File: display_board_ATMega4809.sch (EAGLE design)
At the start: 38 parts, among them J2 LD09P33E4GV00LF, J3 SULLINS_NREC005SABC-M30RCSULL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, SW1 TE_CONNECTIVITY_FSM2JSMAATE_C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, SW2 TE_CONNECTIVITY_FSM2JSMAATE_C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, SW3 TE_CONNECTIVITY_FSM2JSMAATE_C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, SW4 TE_CONNECTIVITY_FSM2JSMAATE_C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, U1 LSF0102DCTR, U2 MCP1703AT-5002E_CB, U3 MCP1801T-3302I_OT, U4 SI2323DDS-T1-GE3SOT_DS-T1-GE3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

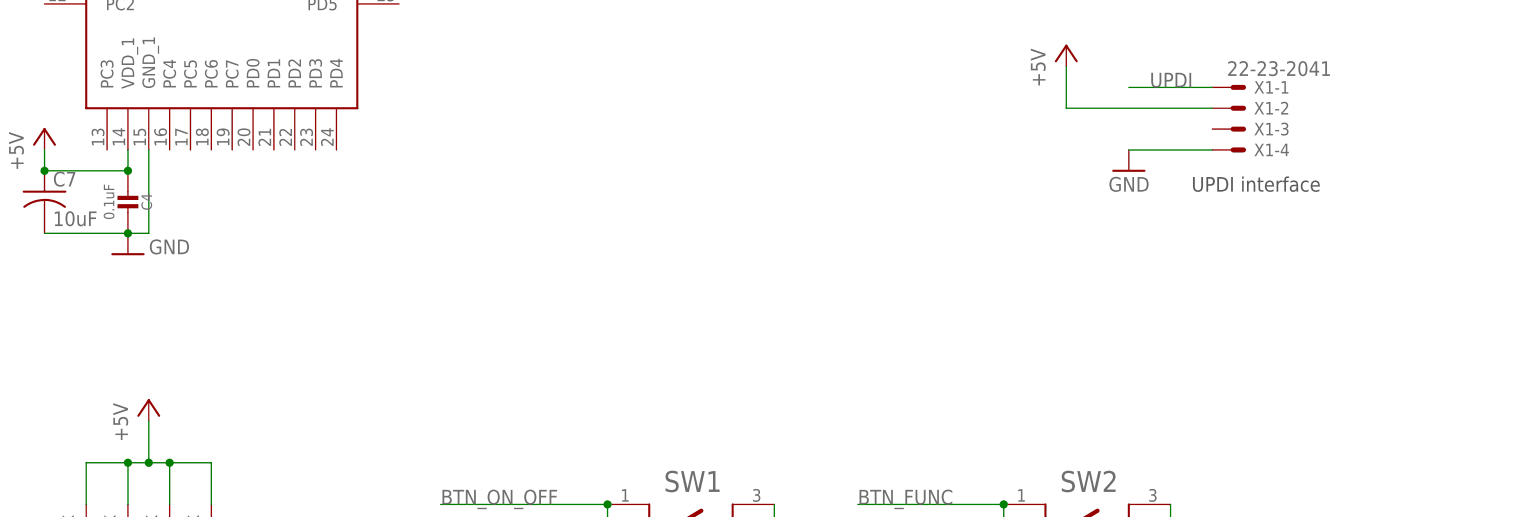
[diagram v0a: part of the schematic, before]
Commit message: Added debugging UART connector
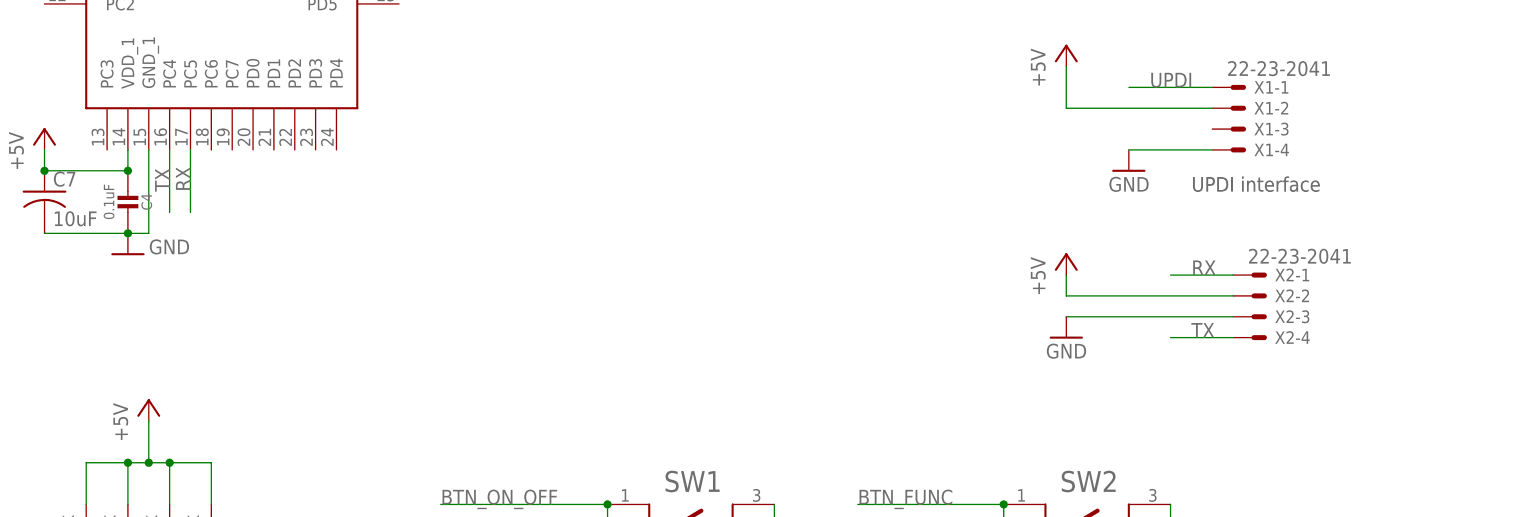
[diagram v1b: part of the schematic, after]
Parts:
- added X2: 22-23-2041, con-molex:22-23-2041
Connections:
- new net RX: U5.PC5, X2-1.S
- new net TX: U5.PC4, X2-4.S
- net +5V: now also X2-2.S
- net GND: now also X2-3.S
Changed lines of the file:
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@@
 <part name="P+11" library="supply1" deviceset="+5V" device=""/>
 <part name="P+12" library="supply1" deviceset="+5V" device=""/>
+<part name="X2" library="con-molex" library_urn="urn:adsk.eagle:library:165" deviceset="22-23-2041" device="" package3d_urn="urn:adsk.eagle:package:8078635/1"/>
+<part name="P+13" library="supply1" deviceset="+5V" device=""/>
+<part name="GND15" library="supply1" library_urn="urn:adsk.eagle:library:371" deviceset="GND" device=""/>
 </parts>
 <sheets>
@@
 <attribute name="VALUE" x="104.14" y="-53.34" size="1.778" layer="96" rot="R90"/>
 </instance>
+<instance part="X2" gate="-1" x="241.3" y="-33.02" smashed="yes">
+<attribute name="NAME" x="243.84" y="-33.782" size="1.524" layer="95"/>
+<attribute name="VALUE" x="240.538" y="-31.623" size="1.778" layer="96"/>
+</instance>
+<instance part="X2" gate="-2" x="241.3" y="-35.56" smashed="yes">
+<attribute name="NAME" x="243.84" y="-36.322" size="1.524" layer="95"/>
+</instance>
+<instance part="X2" gate="-3" x="241.3" y="-38.1" smashed="yes">
+<attribute name="NAME" x="243.84" y="-38.862" size="1.524" layer="95"/>
+</instance>
+<instance part="X2" gate="-4" x="241.3" y="-40.64" smashed="yes">
+<attribute name="NAME" x="243.84" y="-41.402" size="1.524" layer="95"/>
+</instance>
+<instance part="P+13" gate="1" x="218.44" y="-30.48" smashed="yes">
+<attribute name="VALUE" x="215.9" y="-35.56" size="1.778" layer="96" rot="R90"/>
+</instance>
+<instance part="GND15" gate="1" x="218.44" y="-40.64" smashed="yes" rot="MR0">
+<attribute name="VALUE" x="220.98" y="-43.18" size="1.778" layer="96" rot="MR0"/>
+</instance>
 </instances>
 <busses>
@@
 <pinref part="X1" gate="-4" pin="S"/>
 <wire x1="226.06" y1="-17.78" x2="236.22" y2="-17.78" width="0.1524" layer="91"/>
+</segment>
+<segment>
+<pinref part="X2" gate="-3" pin="S"/>
+<pinref part="GND15" gate="1" pin="GND"/>
+<wire x1="238.76" y1="-38.1" x2="218.44" y2="-38.1" width="0.1524" layer="91"/>
 </segment>
 </net>
@@
 <junction x="116.84" y="73.66"/>
 </segment>
+<segment>
+<pinref part="P+13" gate="1" pin="+5V"/>
+<wire x1="218.44" y1="-33.02" x2="218.44" y2="-35.56" width="0.1524" layer="91"/>
+<pinref part="X2" gate="-2" pin="S"/>
+<wire x1="218.44" y1="-35.56" x2="238.76" y2="-35.56" width="0.1524" layer="91"/>
+</segment>
 </net>
 <net name="N$4" class="0">
@@
 </segment>
 </net>
+<net name="TX" class="0">
+<segment>
+<pinref part="U5" gate="G$1" pin="PC4"/>
+<wire x1="109.22" y1="-17.78" x2="109.22" y2="-25.4" width="0.1524" layer="91"/>
+<label x="109.22" y="-22.86" size="1.778" layer="95" rot="R90"/>
+</segment>
+<segment>
+<pinref part="X2" gate="-4" pin="S"/>
+<wire x1="238.76" y1="-40.64" x2="231.14" y2="-40.64" width="0.1524" layer="91"/>
+<label x="233.68" y="-40.64" size="1.778" layer="95"/>
+</segment>
+</net>
+<net name="RX" class="0">
+<segment>
+<pinref part="U5" gate="G$1" pin="PC5"/>
+<wire x1="111.76" y1="-17.78" x2="111.76" y2="-25.4" width="0.1524" layer="91"/>
+<label x="111.76" y="-22.86" size="1.778" layer="95" rot="R90"/>
+</segment>
+<segment>
+<pinref part="X2" gate="-1" pin="S"/>
+<wire x1="238.76" y1="-33.02" x2="231.14" y2="-33.02" width="0.1524" layer="91"/>
+<label x="233.68" y="-33.02" size="1.778" layer="95"/>
+</segment>
+</net>

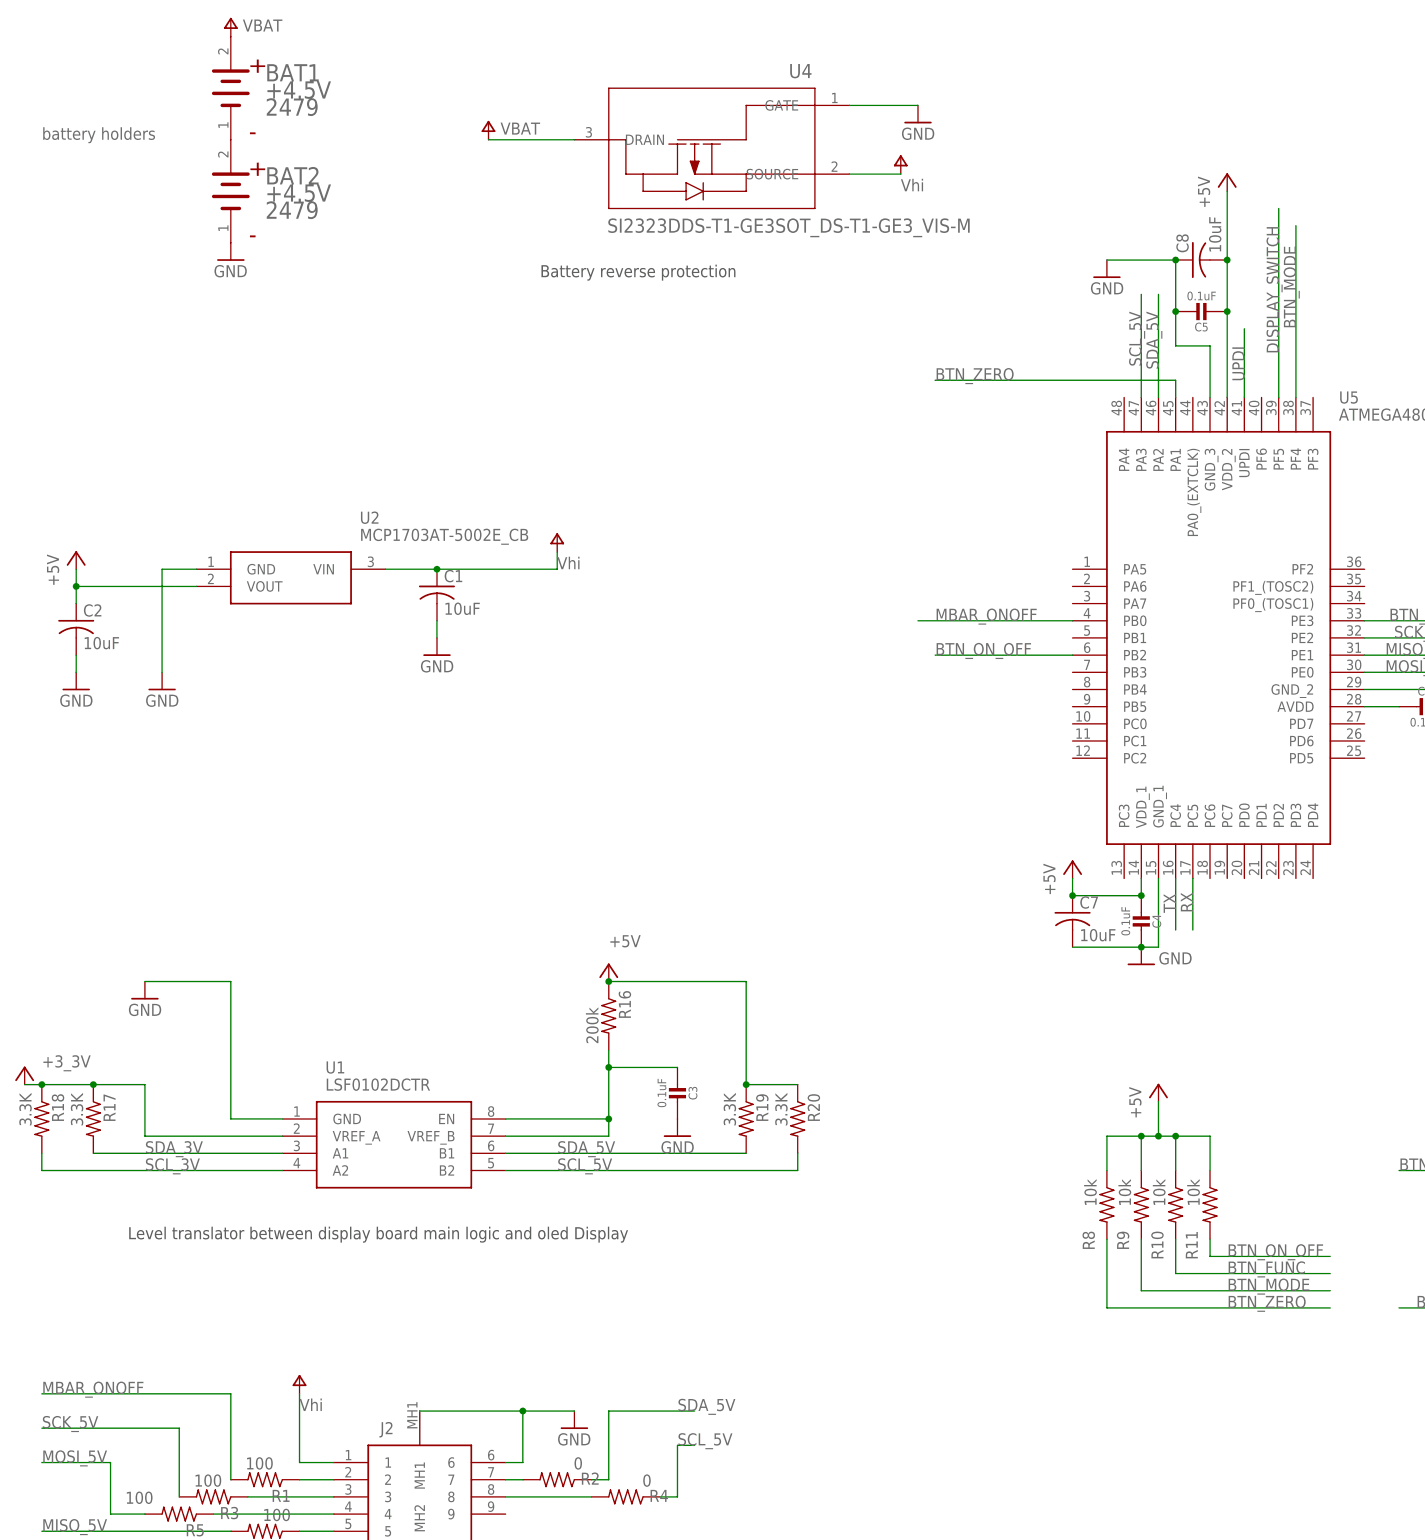
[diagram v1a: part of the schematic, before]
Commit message: Updated the schematic and initial layout commit
- Removed the reverse protection PMOS to reduce power consumption(battery holder has mechanical protection already)
- Initial commit for the layout
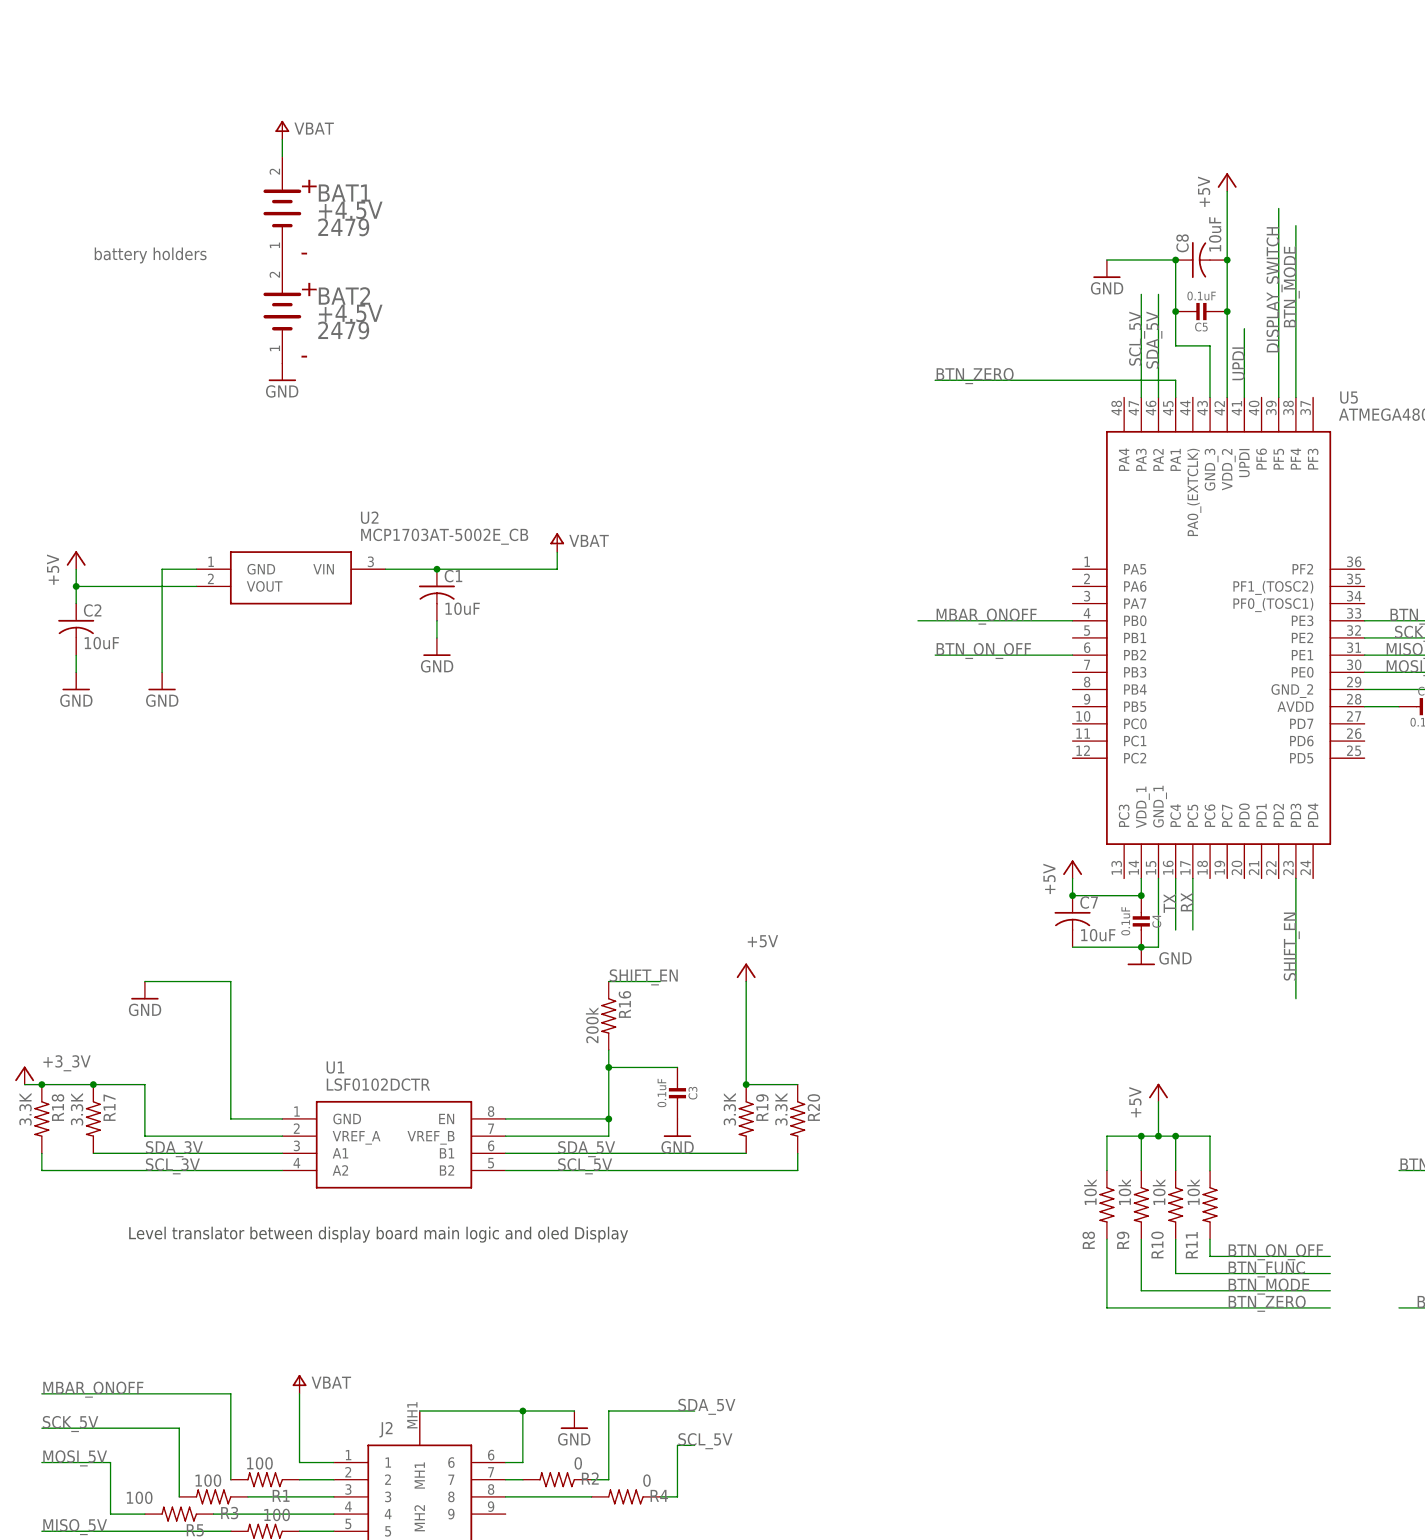
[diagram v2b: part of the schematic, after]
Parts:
- removed U4: SI2323DDS-T1-GE3SOT_DS-T1-GE3_VIS-M, weightScale:SI2323DDS-T1-GE3SOT_DS-T1-GE3_VIS-M
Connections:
- removed net +3V: R17.1, R18.1, U1.VREF_A
- removed net V+: BAT1.ANODE, C1.1, J2.1, U2.VIN, U4.DRAIN, U4.SOURCE
- new net SHIFT_EN: R16.1, U5.PD3
- new net VBAT: BAT1.ANODE, C1.1, J2.1, U2.VIN
- net +3V3: now also R17.1, R18.1, U1.VREF_A
- net +5V: no longer R16.1
- net GND: no longer U4.GATE
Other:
- note removed: "Battery reverse protection"
- moved on the sheet: BAT1, BAT2

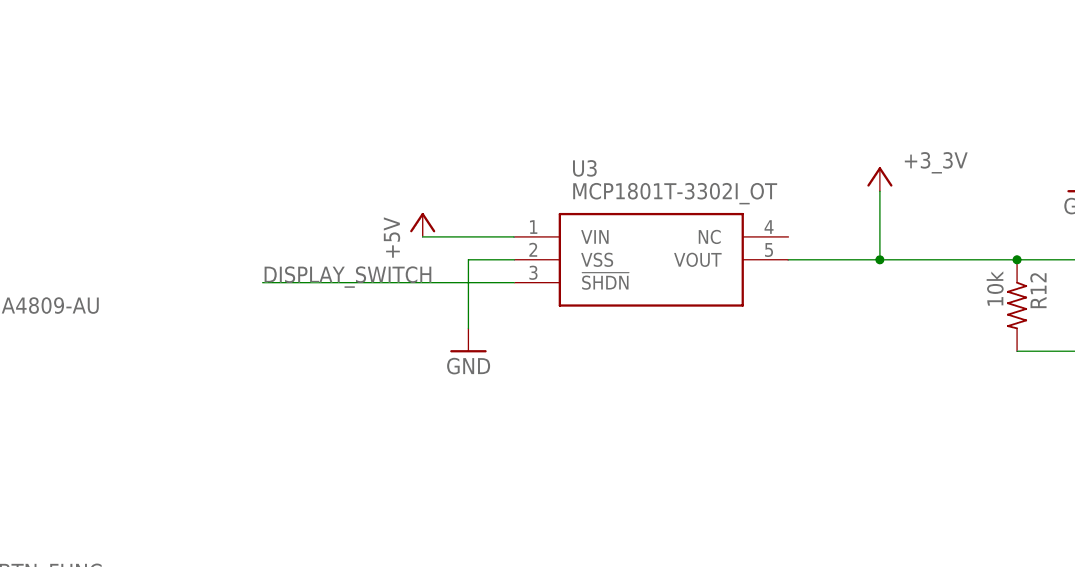
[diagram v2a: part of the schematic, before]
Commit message: Adding decoupling capacitors
-Added decoupling capacitors on OLED LDO
-Added BOM file
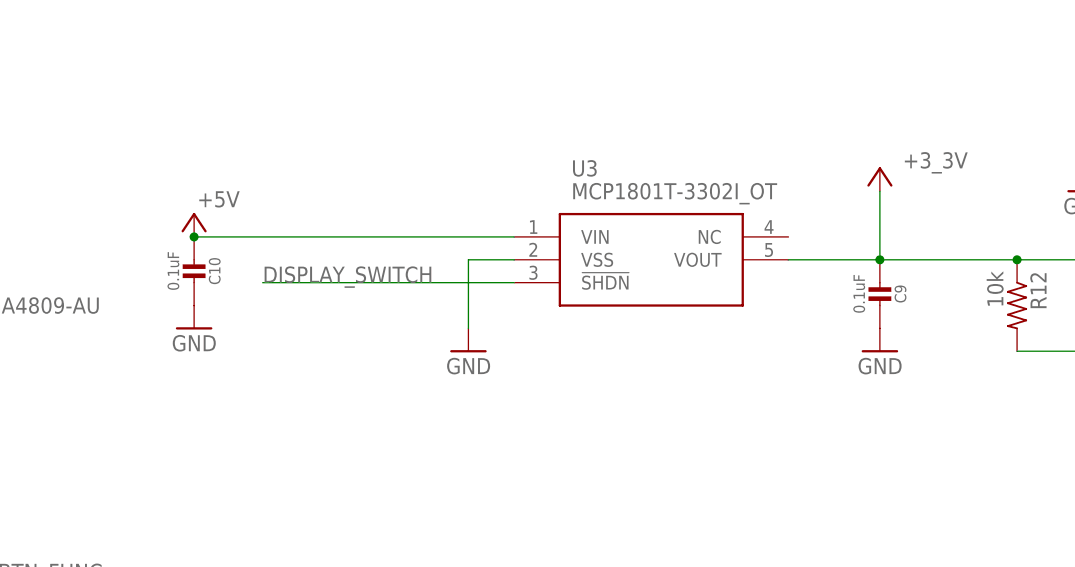
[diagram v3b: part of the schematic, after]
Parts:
- added C10, C9: 0.1uF, microbuilder:CAP_CERAMIC_0603MP
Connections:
- net +3V3: now also C9.2
- net +5V: now also C10.2
- net GND: now also C10.1, C9.1
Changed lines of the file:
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@@
 <part name="GND15" library="supply1" library_urn="urn:adsk.eagle:library:371" deviceset="GND" device=""/>
 <part name="P+3" library="supply1" library_urn="urn:adsk.eagle:library:371" deviceset="V+" device="" value="VBAT"/>
+<part name="C9" library="microbuilder" deviceset="CAP_CERAMIC" device="_0603MP" value="0.1uF"/>
+<part name="GND3" library="supply1" library_urn="urn:adsk.eagle:library:371" deviceset="GND" device=""/>
+<part name="C10" library="microbuilder" deviceset="CAP_CERAMIC" device="_0603MP" value="0.1uF"/>
+<part name="GND16" library="supply1" library_urn="urn:adsk.eagle:library:371" deviceset="GND" device=""/>
 </parts>
 <sheets>
@@
 <attribute name="VALUE" x="204.47" y="63.5" size="1.778" layer="96" align="center-left"/>
 </instance>
-<instance part="P+5" gate="1" x="187.96" y="60.96" smashed="yes">
-<attribute name="VALUE" x="185.42" y="55.88" size="1.778" layer="96" rot="R90"/>
+<instance part="P+5" gate="1" x="162.56" y="60.96" smashed="yes">
+<attribute name="VALUE" x="167.64" y="63.5" size="1.778" layer="96" rot="R180"/>
 </instance>
 <instance part="+3V2" gate="G$1" x="238.76" y="66.04" smashed="yes">
@@
 <instance part="P+3" gate="1" x="-20.32" y="-91.44" smashed="yes">
 <attribute name="VALUE" x="-12.7" y="-91.44" size="1.778" layer="96" rot="R180"/>
+</instance>
+<instance part="C9" gate="G$1" x="238.76" y="53.34" smashed="yes" rot="R180">
+<attribute name="NAME" x="241.05" y="52.09" size="1.27" layer="95" font="vector" rot="R270" align="center"/>
+<attribute name="VALUE" x="236.46" y="52.09" size="1.27" layer="96" font="vector" rot="R270" align="center"/>
+</instance>
+<instance part="GND3" gate="1" x="238.76" y="45.72" smashed="yes" rot="MR0">
+<attribute name="VALUE" x="241.3" y="43.18" size="1.778" layer="96" rot="MR0"/>
+</instance>
+<instance part="C10" gate="G$1" x="162.56" y="55.88" smashed="yes" rot="R180">
+<attribute name="NAME" x="164.85" y="54.63" size="1.27" layer="95" font="vector" rot="R270" align="center"/>
+<attribute name="VALUE" x="160.26" y="54.63" size="1.27" layer="96" font="vector" rot="R270" align="center"/>
+</instance>
+<instance part="GND16" gate="1" x="162.56" y="48.26" smashed="yes" rot="MR0">
+<attribute name="VALUE" x="165.1" y="45.72" size="1.778" layer="96" rot="MR0"/>
 </instance>
 </instances>
@@
 <wire x1="238.76" y1="-38.1" x2="218.44" y2="-38.1" width="0.1524" layer="91"/>
 </segment>
+<segment>
+<pinref part="C9" gate="G$1" pin="1"/>
+<pinref part="GND3" gate="1" pin="GND"/>
+</segment>
+<segment>
+<pinref part="C10" gate="G$1" pin="1"/>
+<pinref part="GND16" gate="1" pin="GND"/>
+</segment>
 </net>
 <net name="N$2" class="0">
@@
 <pinref part="U3" gate="G$1" pin="VIN"/>
 <pinref part="P+5" gate="1" pin="+5V"/>
-<wire x1="198.12" y1="58.42" x2="187.96" y2="58.42" width="0.1524" layer="91"/>
+<wire x1="198.12" y1="58.42" x2="162.56" y2="58.42" width="0.1524" layer="91"/>
+<pinref part="C10" gate="G$1" pin="2"/>
+<junction x="162.56" y="58.42"/>
 </segment>
 <segment>
@@
 <junction x="238.76" y="55.88"/>
 <pinref part="+3V2" gate="G$1" pin="+3V3"/>
-</segment>
-<segment>
+<pinref part="C9" gate="G$1" pin="2"/>
+</segment>
+<segment>
